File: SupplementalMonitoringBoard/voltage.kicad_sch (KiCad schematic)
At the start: 5 parts, among them U1 OPA842xDBV

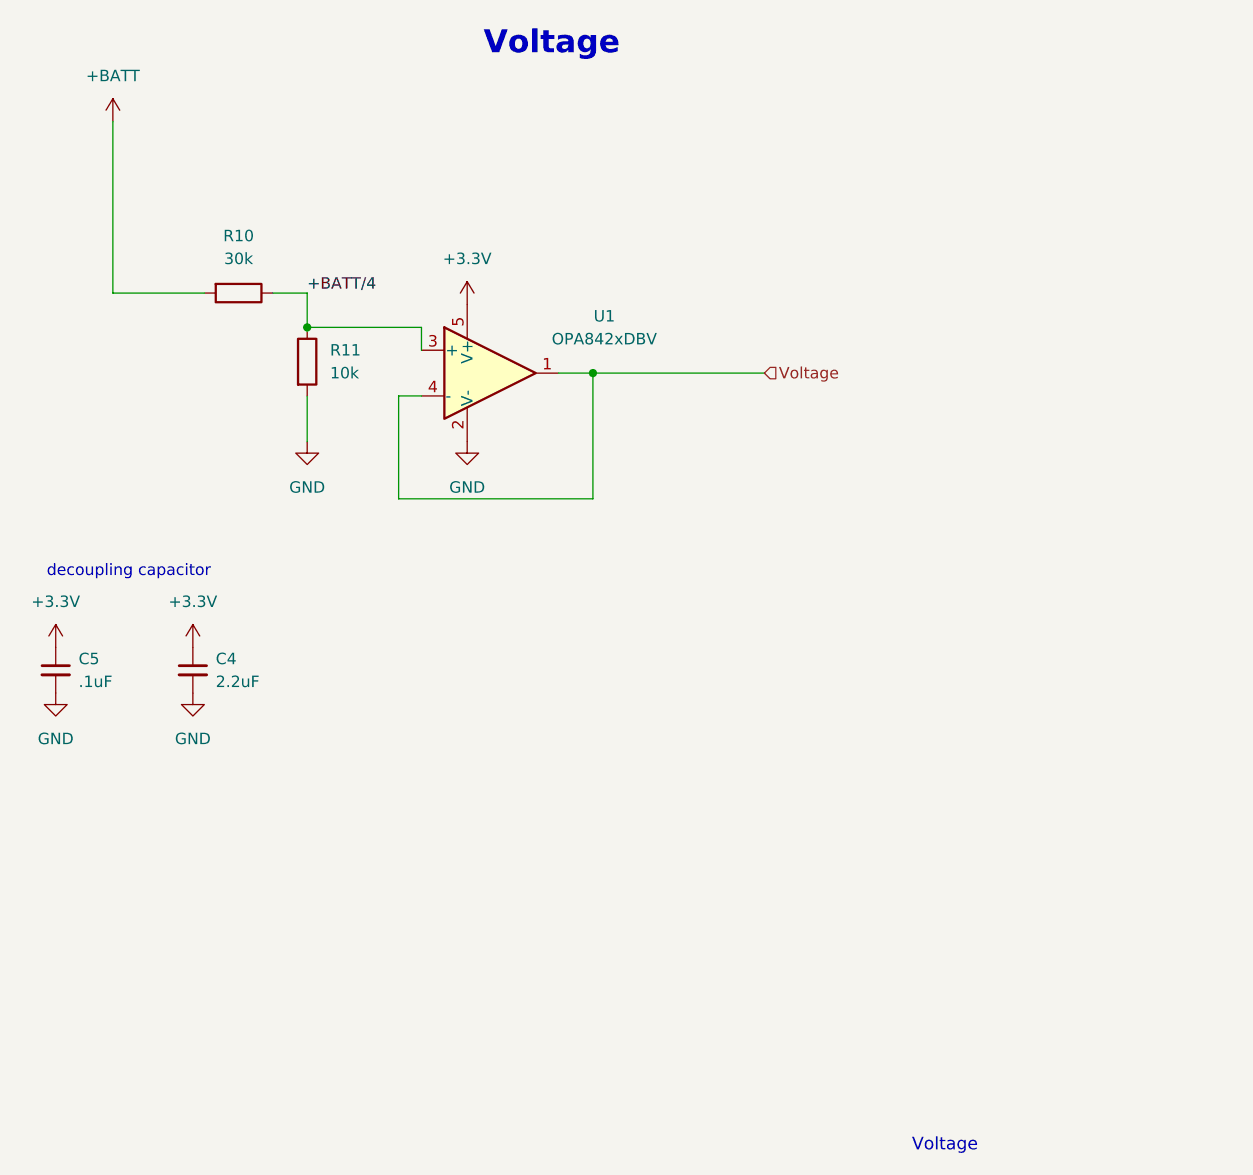
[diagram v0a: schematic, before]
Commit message: Adressed Reviews - Supplemental Monitoring Board
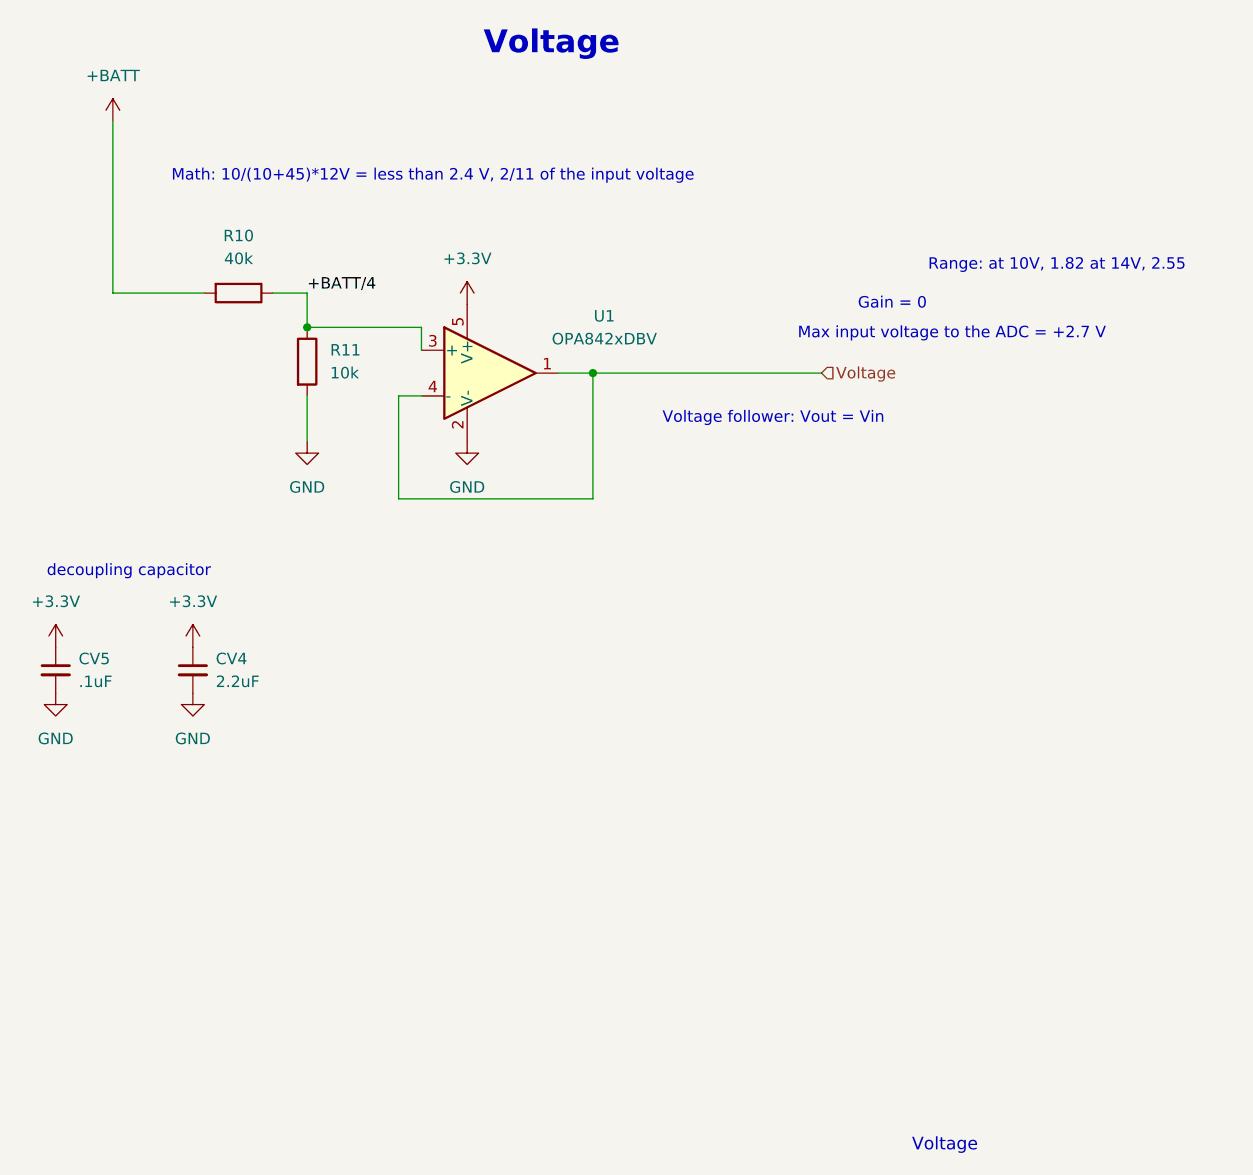
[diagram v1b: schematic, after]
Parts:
- R10: value 30k -> 40k
- renumbered C4 to CV4, C5 to CV5
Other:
- note added: "Gain = 0"
- note added: "Math: 10/(10+45)*12V = less than 2.4 V, 2/11 of the input voltage"
- note added: "Max input voltage to the ADC = +2.7 V"
- note added: "Range: at 10V, 1.82 at 14V, 2.55"
- note added: "Voltage follower: Vout = Vin"
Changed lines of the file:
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@@
 	(wire
 		(pts
-			(xy 151.13 104.14) (xy 170.18 104.14)
+			(xy 151.13 104.14) (xy 176.53 104.14)
 		)
 		(stroke
@@
 			(width 0)
 			(type default)
+		)
+	)
+	(text "Max input voltage to the ADC = +2.7 V\n\n"
+		(exclude_from_sim no)
+		(at 191.008 100.838 0)
+		(effects
+			(font
+				(size 1.27 1.27)
+			)
 		)
 	)
@@
 		)
 	)
+	(text "Voltage follower: Vout = Vin\n\n"
+		(exclude_from_sim no)
+		(at 171.196 110.236 0)
+		(effects
+			(font
+				(size 1.27 1.27)
+			)
+		)
+	)
 	(text "Voltage"
 		(exclude_from_sim no)
@@
 		)
 	)
+	(text "Math: 10/(10+45)*12V = less than 2.4 V, 2/11 of the input voltage\n"
+		(exclude_from_sim no)
+		(at 133.35 82.296 0)
+		(effects
+			(font
+				(size 1.27 1.27)
+			)
+		)
+	)
+	(text "Gain = 0\n"
+		(exclude_from_sim no)
+		(at 184.404 96.52 0)
+		(effects
+			(font
+				(size 1.27 1.27)
+			)
+		)
+	)
+	(text "Range: at 10V, 1.82 at 14V, 2.55"
+		(exclude_from_sim no)
+		(at 202.692 92.202 0)
+		(effects
+			(font
+				(size 1.27 1.27)
+			)
+		)
+	)
 	(text "decoupling capacitor"
 		(exclude_from_sim no)
@@
 	(hierarchical_label "Voltage"
 		(shape input)
-		(at 170.18 104.14 0)
+		(at 176.53 104.14 0)
 		(fields_autoplaced yes)
 		(effects
@@
 		(dnp no)
 		(fields_autoplaced yes)
-		(property "Reference" "C5"
+		(property "Reference" "CV5"
 			(at 93.98 135.8962 0)
 			(effects
@@
 			(project "SupplementalMonitoringBoard"
 				(path "/aa0415d0-3287-4bc4-9a8e-766ada9ace2f/c3517b11-42d4-41ac-8608-60dda8052ca3"
-					(reference "C5")
+					(reference "CV5")
 					(unit 1)
 				)
@@
 			)
 		)
-		(property "Value" "30k"
+		(property "Value" "40k"
 			(at 111.76 91.44 90)
 			(effects
@@
 		(dnp no)
 		(fields_autoplaced yes)
-		(property "Reference" "C4"
+		(property "Reference" "CV4"
 			(at 109.22 135.8962 0)
 			(effects
@@
 			(project "SupplementalMonitoringBoard"
 				(path "/aa0415d0-3287-4bc4-9a8e-766ada9ace2f/c3517b11-42d4-41ac-8608-60dda8052ca3"
-					(reference "C4")
-					(unit 1)
-				)
+					(reference "CV4")
+					(unit 1)
+				)

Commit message: Supplemental MOnitoring Board
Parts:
- CV4: P/N (none) -> UMK212ABJ225KG-T
- CV5: value .1uF -> 1nF; P/N (none) -> C0805C102J5HACAUTO
- R10: P/N (none) -> CRCW080540K0FKEA
- R11: P/N (none) -> CRCW080510K0FKEAC
- U1: P/N (none) -> SBOS267D
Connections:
- net +BATT renamed +12V
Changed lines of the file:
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@@
 			)
 		)
-		(property "Value" ".1uF"
+		(property "Value" "1nF"
 			(at 93.98 138.4362 0)
 			(effects
@@
 			)
 		)
-		(property "Datasheet" "~"
+		(property "Datasheet" "https://www.mouser.com/ProductDetail/KEMET/C0805C102J5HACAUTO?qs=j%252B1pi9TdxUbgwPgoM1tuTw%3D%3D"
 			(at 91.44 137.16 0)
 			(effects
@@
 		)
 		(property "Description" "Unpolarized capacitor, small symbol"
+			(at 91.44 137.16 0)
+			(effects
+				(font
+					(size 1.27 1.27)
+				)
+				(hide yes)
+			)
+		)
+		(property "P/N" "C0805C102J5HACAUTO"
 			(at 91.44 137.16 0)
 			(effects
@@
 			)
 		)
-		(property "Datasheet" "~"
+		(property "Datasheet" "https://www.vishay.com/docs/20035/dcrcwe3.pdf"
 			(at 111.76 95.25 0)
 			(effects
@@
 		)
 		(property "Description" "Resistor"
+			(at 111.76 95.25 0)
+			(effects
+				(font
+					(size 1.27 1.27)
+				)
+				(hide yes)
+			)
+		)
+		(property "P/N" "CRCW080540K0FKEA"
 			(at 111.76 95.25 0)
 			(effects
@@
 			)
 		)
+		(property "P/N" "SBOS267D"
+			(at 139.7 104.14 0)
+			(effects
+				(font
+					(size 1.27 1.27)
+				)
+				(hide yes)
+			)
+		)
 		(pin "2"
 		)
@@
 	)
 	(symbol
-		(lib_id "power:+BATT")
+		(lib_id "power:+12V")
 		(at 97.79 76.2 0)
 		(unit 1)
@@
 			)
 		)
-		(property "Value" "+BATT"
+		(property "Value" "+12V"
 			(at 97.79 71.12 0)
 			(effects
@@
 			)
 		)
-		(property "Description" "Power symbol creates a global label with name \"+BATT\""
+		(property "Description" "Power symbol creates a global label with name \"+12V\""
 			(at 97.79 76.2 0)
 			(effects
@@
 		)
 		(instances
-			(project "SupplementalMonitoringBoard"
+			(project ""
 				(path "/aa0415d0-3287-4bc4-9a8e-766ada9ace2f/c3517b11-42d4-41ac-8608-60dda8052ca3"
 					(reference "#PWR07")
@@
 			)
 		)
-		(property "Datasheet" "~"
+		(property "Datasheet" "https://www.mouser.com/datasheet/2/447/PYu_RT_1_to_0_01_RoHS_L_15-3461507.pdf"
 			(at 119.38 102.87 0)
 			(effects
@@
 		)
 		(property "Description" "Resistor"
+			(at 119.38 102.87 0)
+			(effects
+				(font
+					(size 1.27 1.27)
+				)
+				(hide yes)
+			)
+		)
+		(property "P/N" "CRCW080510K0FKEAC"
 			(at 119.38 102.87 0)
 			(effects
@@
 			)
 		)
-		(property "Datasheet" "~"
+		(property "Datasheet" "https://www.mouser.com/ProductDetail/Murata-Electronics/GRM219R6YA475KA73D?qs=eeBpzGFlv%252B%252Bho6epIC%2FPCA%3D%3D"
 			(at 106.68 137.16 0)
 			(effects
@@
 			(at 106.68 137.16 0)
 			(effects
+				(font
+					(size 1.27 1.27)
+				)
+				(hide yes)
+			)
+		)
+		(property "P/N" "UMK212ABJ225KG-T"
+			(at 106.68 137.16 0)
+			(effects

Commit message: Supplemental Monitoring Board
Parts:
- R11: P/N CRCW080510K0FKEAC -> RT0603FRE0710KL
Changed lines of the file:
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@@
 			)
 		)
-		(property "Datasheet" "https://www.mouser.com/datasheet/2/447/PYu_RT_1_to_0_01_RoHS_L_15-3461507.pdf"
+		(property "Datasheet" "https://www.mouser.com/ProductDetail/603-RT0603FRE0710KL"
 			(at 119.38 102.87 0)
 			(effects
@@
 			)
 		)
-		(property "P/N" "CRCW080510K0FKEAC"
+		(property "P/N" "RT0603FRE0710KL "
 			(at 119.38 102.87 0)
 			(effects
